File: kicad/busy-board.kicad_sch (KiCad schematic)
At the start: 40 parts, among them SW101 MAN_CNT, SW102 CLK_SELECT, U101 LM393, U102 LM393, U103 4040, U104 LM393

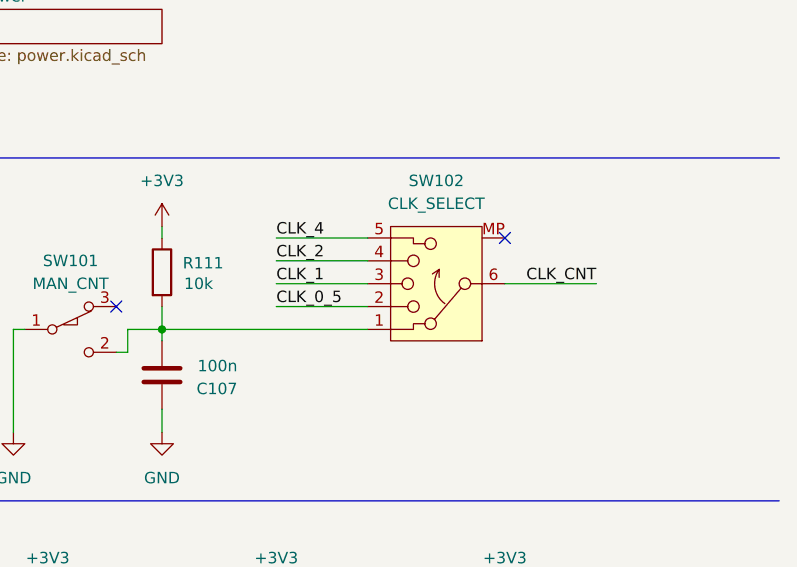
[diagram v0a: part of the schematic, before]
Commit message: Fix v1 issues
- Change BJT to MOSFET for LED control: voltage drop on PWM
- Change voltage switch to PWM switch for 7-seg and bar control
- Change LDO to limit drop-out with battery
- Decrease resistor on Purple LED to increase luminosity
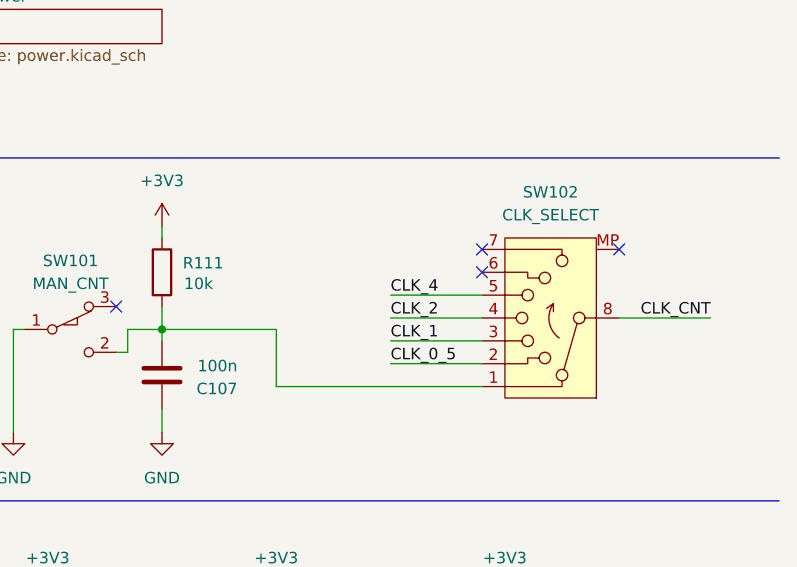
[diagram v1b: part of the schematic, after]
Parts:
- SW102: symbol Switch:SW_Rotary_1x5_MP -> Switch:SW_Rotary_1x7_MP
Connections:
- net CLK_CNT: now also SW102.8; no longer SW102.6
- no-connect marks 11 -> 13
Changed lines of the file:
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@@
 	(title_block
 		(title "Busy Board")
-		(date "2026-08-08")
-		(rev "1.0.0")
+		(date "2026-09-25")
+		(rev "1.1.0")
 	)
 	(text_box "Sawtooth generator:\nT_128 = 7.8ms\nT = R * C \n  = 10k * 100n \n  = 1ms << T_128"
@@
 	)
 	(no_connect
+		(at 251.46 101.6)
+	)
+	(no_connect
 		(at 74.93 116.84)
 	)
 	(no_connect
-		(at 254 97.79)
+		(at 266.7 99.06)
+	)
+	(no_connect
+		(at 251.46 99.06)
 	)
 	(no_connect
@@
 	(wire
 		(pts
-			(xy 215.9 107.95) (xy 238.76 107.95)
-		)
-		(stroke
-			(width 0)
-			(type default)
-		)
-	)
-	(wire
-		(pts
 			(xy 63.5 116.84) (xy 74.93 116.84)
 		)
@@
 	(wire
 		(pts
-			(xy 228.6 102.87) (xy 238.76 102.87)
+			(xy 241.3 109.22) (xy 251.46 109.22)
 		)
 		(stroke
@@
 	(wire
 		(pts
+			(xy 228.6 107.95) (xy 215.9 107.95)
+		)
+		(stroke
+			(width 0)
+			(type default)
+		)
+	)
+	(wire
+		(pts
 			(xy 196.85 139.7) (xy 203.2 139.7)
 		)
@@
 	(wire
 		(pts
-			(xy 228.6 105.41) (xy 238.76 105.41)
-		)
-		(stroke
-			(width 0)
-			(type default)
-		)
-	)
-	(wire
-		(pts
 			(xy 27.94 62.23) (xy 27.94 64.77)
 		)
@@
 	(wire
 		(pts
+			(xy 241.3 111.76) (xy 251.46 111.76)
+		)
+		(stroke
+			(width 0)
+			(type default)
+		)
+	)
+	(wire
+		(pts
 			(xy 130.81 73.66) (xy 133.35 73.66)
 		)
@@
 	(wire
 		(pts
-			(xy 228.6 97.79) (xy 238.76 97.79)
+			(xy 241.3 104.14) (xy 251.46 104.14)
 		)
 		(stroke
@@
 	(wire
 		(pts
+			(xy 251.46 114.3) (xy 228.6 114.3)
+		)
+		(stroke
+			(width 0)
+			(type default)
+		)
+	)
+	(wire
+		(pts
 			(xy 101.6 74.93) (xy 101.6 80.01)
 		)
@@
 	(wire
 		(pts
-			(xy 254 102.87) (xy 264.16 102.87)
+			(xy 266.7 106.68) (xy 276.86 106.68)
 		)
 		(stroke
@@
 	(wire
 		(pts
+			(xy 228.6 114.3) (xy 228.6 107.95)
+		)
+		(stroke
+			(width 0)
+			(type default)
+		)
+	)
+	(wire
+		(pts
 			(xy 214.63 26.67) (xy 229.87 26.67)
 		)
@@
 	(wire
 		(pts
-			(xy 228.6 100.33) (xy 238.76 100.33)
+			(xy 241.3 106.68) (xy 251.46 106.68)
 		)
 		(stroke
@@
 	)
 	(label "CLK_2"
-		(at 228.6 100.33 0)
+		(at 241.3 106.68 0)
 		(effects
 			(font
@@
 	)
 	(label "CLK_CNT"
-		(at 264.16 102.87 180)
+		(at 276.86 106.68 180)
 		(effects
 			(font
@@
 	)
 	(label "CLK_0_5"
-		(at 228.6 105.41 0)
+		(at 241.3 111.76 0)
 		(effects
 			(font
@@
 	)
 	(label "CLK_4"
-		(at 228.6 97.79 0)
+		(at 241.3 104.14 0)
 		(effects
 			(font
@@
 	)
 	(label "CLK_1"
-		(at 228.6 102.87 0)
+		(at 241.3 109.22 0)
 		(effects
 			(font
@@
 	)
 	(symbol
-		(lib_id "Switch:SW_Rotary_1x5_MP")
-		(at 246.38 102.87 180)
+		(lib_id "Switch:SW_Rotary_1x7_MP")
+		(at 259.08 106.68 180)
 		(unit 1)
 		(exclude_from_sim no)
@@
 		(fields_autoplaced yes)
 		(property "Reference" "SW102"
-			(at 246.38 91.44 0)
+			(at 259.08 92.71 0)
 			(effects
 				(font
@@
 		)
 		(property "Value" "CLK_SELECT"
-			(at 246.38 93.98 0)
+			(at 259.08 95.25 0)
 			(effects
 				(font
@@
 		)
 		(property "Footprint" "footprints:SW-TH_RT-0C4-D"
-			(at 246.38 92.71 0)
+			(at 259.08 96.52 0)
 			(effects
 				(font
@@
 		)
 		(property "Datasheet" "https://www.lcsc.com/datasheet/C508440.pdf"
-			(at 246.38 90.17 0)
+			(at 259.08 93.98 0)
 			(effects
 				(font
@@
 		)
 		(property "Description" "Rotary switch 1x6, SP6T with mount point"
-			(at 246.38 102.87 0)
+			(at 259.08 106.68 0)
 			(effects
 				(font
@@
 		)
 		(property "LCSC Part #" "C508440"
-			(at 246.38 102.87 0)
+			(at 259.08 106.68 0)
 			(effects
 				(font
@@
 		)
 		(property "Manufacturer" "Dailywell"
-			(at 246.38 102.87 0)
+			(at 259.08 106.68 0)
 			(effects
 				(font
@@
 		)
 		(property "MFR Part #" "RT-0C5"
-			(at 246.38 102.87 0)
+			(at 259.08 106.68 0)
 			(effects
 				(font
@@
 		(pin "2"
 		)
+		(pin "8"
+		)
+		(pin "7"
+		)
 		(instances
